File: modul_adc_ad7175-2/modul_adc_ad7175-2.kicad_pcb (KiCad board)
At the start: 2 copper layers, 61 x 55.9 mm, 79 parts

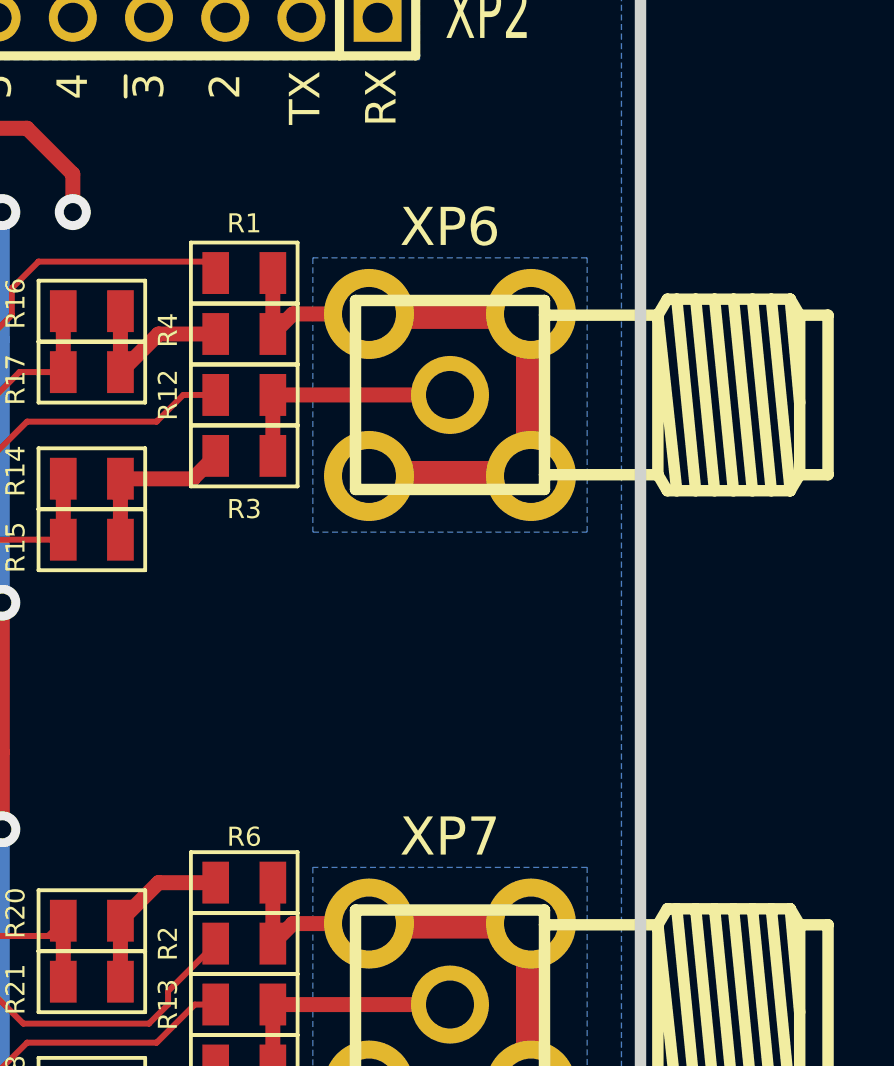
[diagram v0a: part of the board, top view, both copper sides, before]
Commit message: Перевёл проект на Kicad 6.0
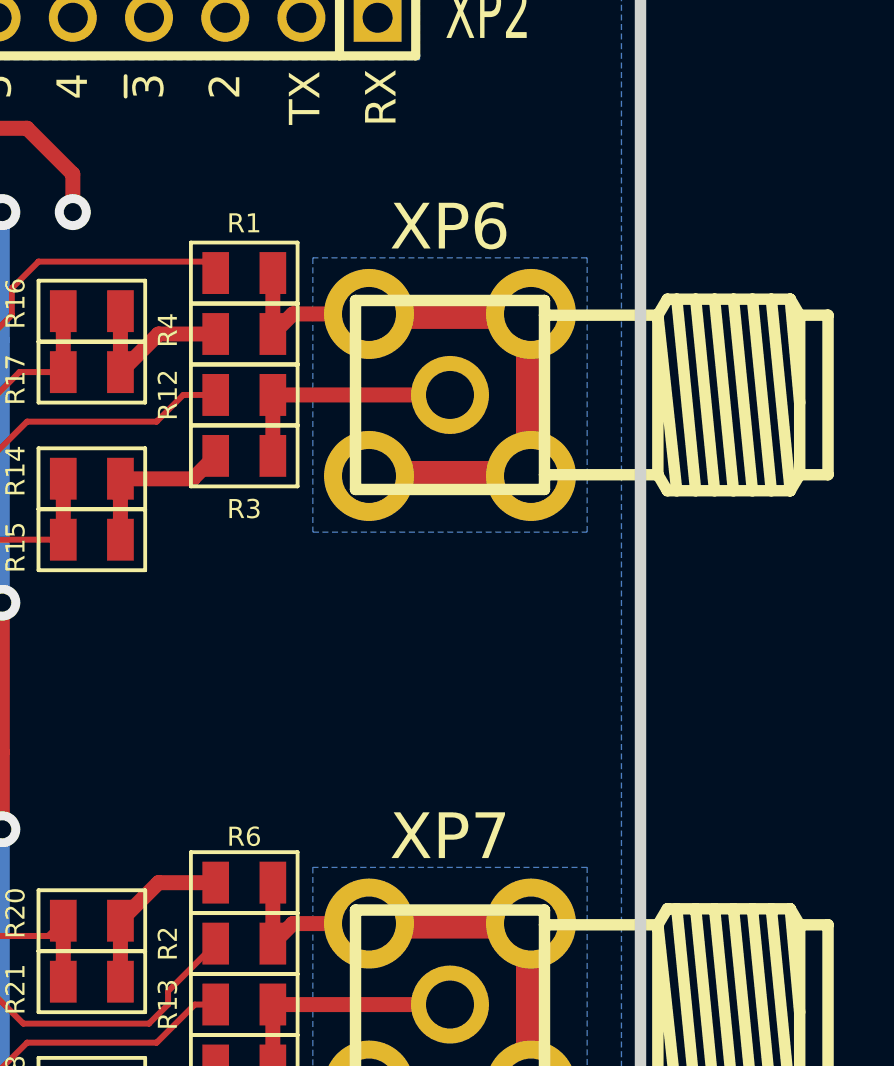
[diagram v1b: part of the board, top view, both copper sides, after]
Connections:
- net /~CS renamed /~{CS}
- net /~SYNC~/ERR renamed /~{SYNC}/ERR
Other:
- net class Default removed
- board text added: "~{10}"
- board text added: "~{11}"
- board text added: "~{3}"
- board text added: "~{5}"
- board text added: "~{6}"
- board text added: "~{9}"
- board text removed: "~10"
- board text removed: "~11"
- board text removed: "~3"
- board text removed: "~5"
- board text removed: "~6"
- board text removed: "~9"
